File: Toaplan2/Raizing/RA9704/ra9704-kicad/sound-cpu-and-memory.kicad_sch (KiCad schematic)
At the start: 10 parts, among them U713 74HC244, U717 74HC367, U74 74HC244, U75 TMPZ84C00AP-8 (Z80), U77 27C020, U78 CY7C185

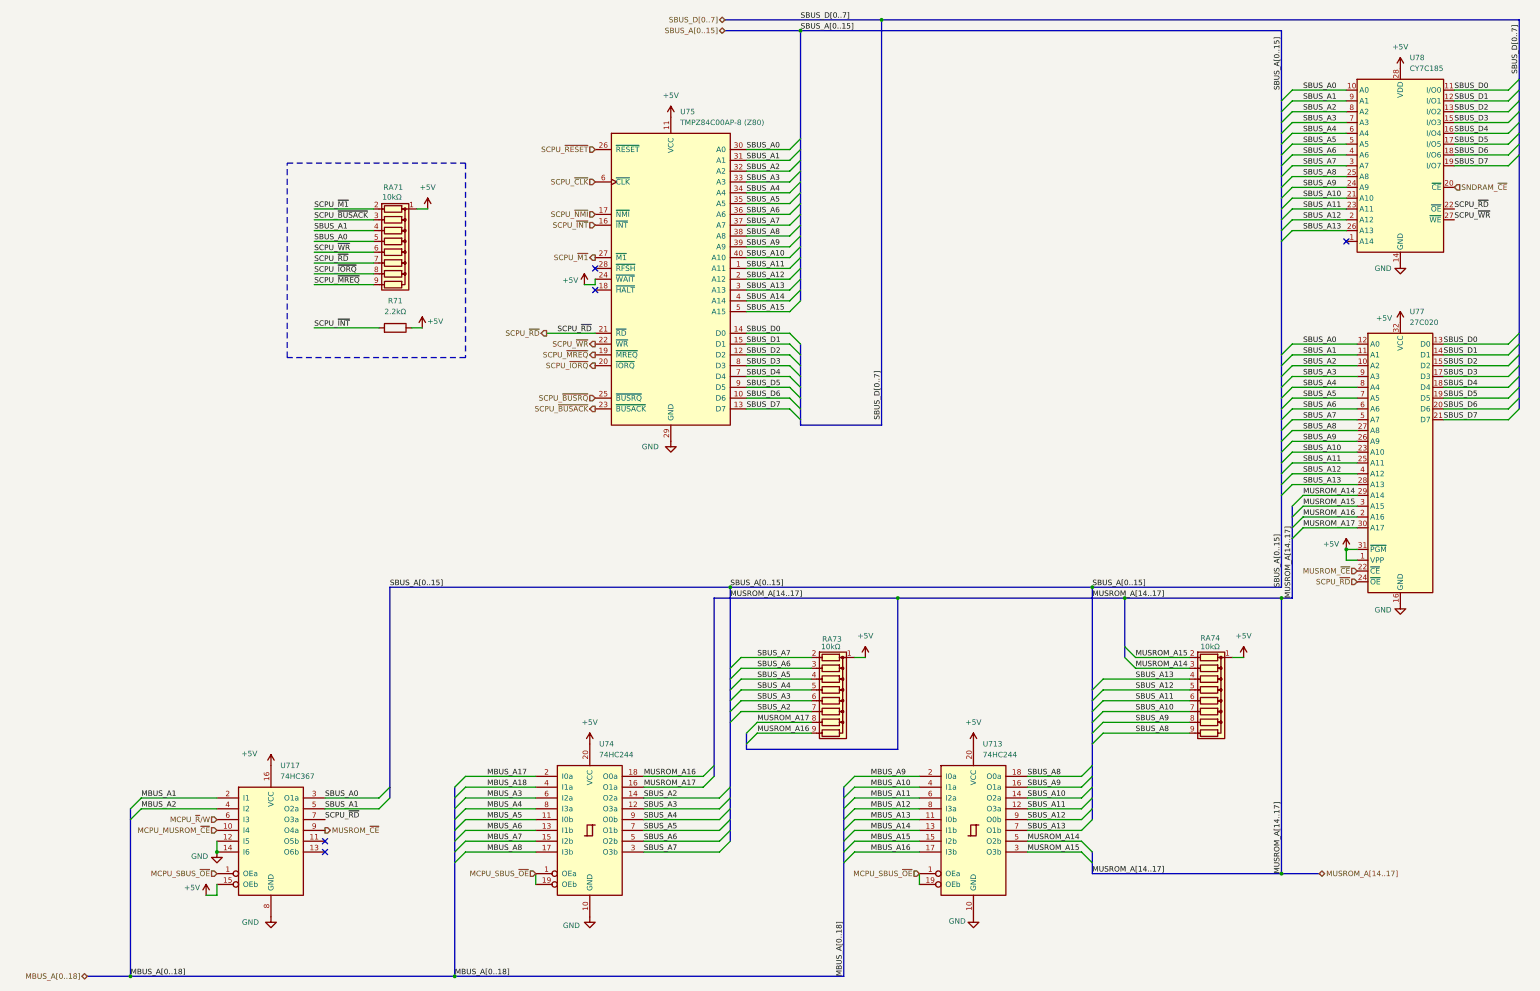
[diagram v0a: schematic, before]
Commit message: fix(ra9704): Add Os as a proxy for 0s in all reference designators
RA9704 has reference designators such that each number has a preceding zero (e.g. RA076, U074, etc.). This causes a bug in KiCAD.

This is 'fixed' by using the 'O' (the letter 'Oh') character instead.

For more info, see the following issue on the KiCAD Gitlab repo

https://gitlab.com/kicad/code/kicad/-/issues/19229
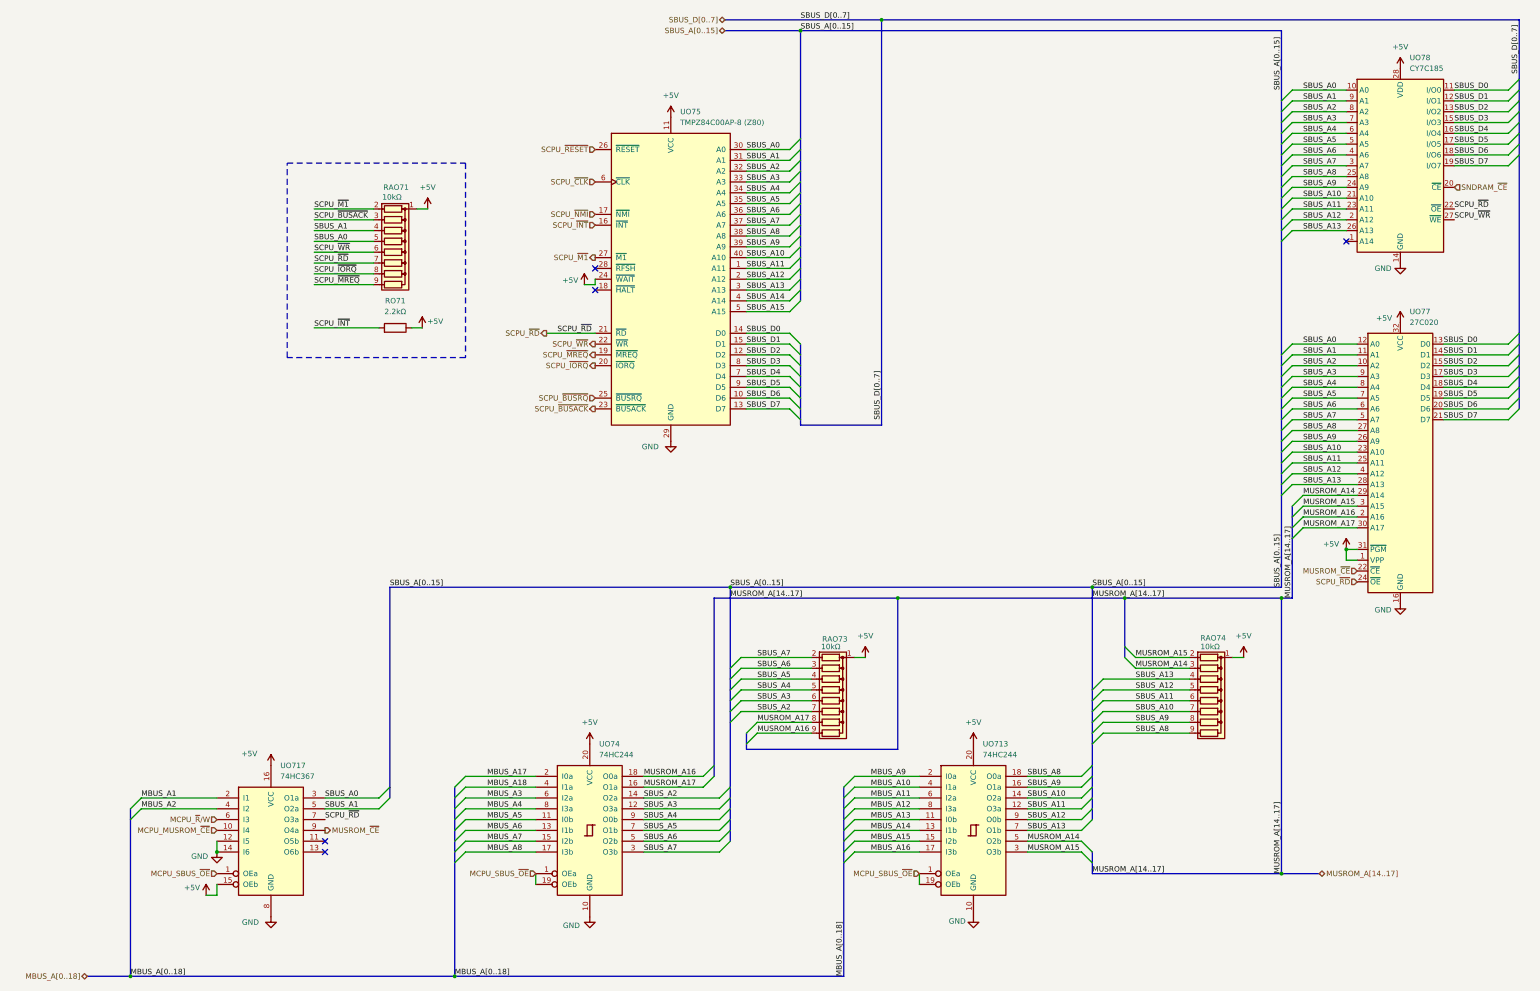
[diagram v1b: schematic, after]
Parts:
- renumbered RA71 to RAO71, RA73 to RAO73, RA74 to RAO74, R71 to RO71, U713 to UO713, U717 to UO717, U74 to UO74, U75 to UO75, U77 to UO77, U78 to UO78
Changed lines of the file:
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@@
 		(dnp no)
 		(fields_autoplaced yes)
-		(property "Reference" "U713"
+		(property "Reference" "UO713"
 			(at 267.6241 189.23 0)
 			(effects
@@
 			(project "ra9704"
 				(path "/24d3b4cf-2360-45fc-8c40-cedc8afdf9e1/44ef47a8-0f29-401a-8a6a-1ae8d653f277"
-					(reference "U713")
+					(reference "UO713")
 					(unit 1)
 				)
@@
 		(dnp no)
 		(fields_autoplaced yes)
-		(property "Reference" "U77"
+		(property "Reference" "UO77"
 			(at 367.9541 87.63 0)
 			(effects
@@
 			(project "ra9704"
 				(path "/24d3b4cf-2360-45fc-8c40-cedc8afdf9e1/44ef47a8-0f29-401a-8a6a-1ae8d653f277"
-					(reference "U77")
+					(reference "UO77")
 					(unit 1)
 				)
@@
 		(on_board yes)
 		(dnp no)
-		(property "Reference" "RA74"
+		(property "Reference" "RAO74"
 			(at 318.77 164.338 90)
 			(effects
@@
 			(project "ra9704"
 				(path "/24d3b4cf-2360-45fc-8c40-cedc8afdf9e1/44ef47a8-0f29-401a-8a6a-1ae8d653f277"
-					(reference "RA74")
+					(reference "RAO74")
 					(unit 1)
 				)
@@
 		(on_board yes)
 		(dnp no)
-		(property "Reference" "RA71"
+		(property "Reference" "RAO71"
 			(at 126.746 58.42 90)
 			(effects
@@
 			(project "ra9704"
 				(path "/24d3b4cf-2360-45fc-8c40-cedc8afdf9e1/44ef47a8-0f29-401a-8a6a-1ae8d653f277"
-					(reference "RA71")
+					(reference "RAO71")
 					(unit 1)
 				)
@@
 		(dnp no)
 		(fields_autoplaced yes)
-		(property "Reference" "U75"
+		(property "Reference" "UO75"
 			(at 196.5041 40.64 0)
 			(effects
@@
 			(project "ra9704"
 				(path "/24d3b4cf-2360-45fc-8c40-cedc8afdf9e1/44ef47a8-0f29-401a-8a6a-1ae8d653f277"
-					(reference "U75")
+					(reference "UO75")
 					(unit 1)
 				)
@@
 		(dnp no)
 		(fields_autoplaced yes)
-		(property "Reference" "U74"
+		(property "Reference" "UO74"
 			(at 177.4541 189.23 0)
 			(effects
@@
 			(project "ra9704"
 				(path "/24d3b4cf-2360-45fc-8c40-cedc8afdf9e1/44ef47a8-0f29-401a-8a6a-1ae8d653f277"
-					(reference "U74")
+					(reference "UO74")
 					(unit 1)
 				)
@@
 		(dnp no)
 		(fields_autoplaced yes)
-		(property "Reference" "U78"
+		(property "Reference" "UO78"
 			(at 367.9541 27.94 0)
 			(effects
@@
 			(project "ra9704"
 				(path "/24d3b4cf-2360-45fc-8c40-cedc8afdf9e1/44ef47a8-0f29-401a-8a6a-1ae8d653f277"
-					(reference "U78")
+					(reference "UO78")
 					(unit 1)
 				)
@@
 		(on_board yes)
 		(dnp no)
-		(property "Reference" "RA73"
+		(property "Reference" "RAO73"
 			(at 229.87 164.592 90)
 			(effects
@@
 			(project "ra9704"
 				(path "/24d3b4cf-2360-45fc-8c40-cedc8afdf9e1/44ef47a8-0f29-401a-8a6a-1ae8d653f277"
-					(reference "RA73")
+					(reference "RAO73")
 					(unit 1)
 				)
@@
 		(dnp no)
 		(fields_autoplaced yes)
-		(property "Reference" "R71"
+		(property "Reference" "RO71"
 			(at 129.54 85.09 90)
 			(effects
@@
 			(project "ra9704"
 				(path "/24d3b4cf-2360-45fc-8c40-cedc8afdf9e1/44ef47a8-0f29-401a-8a6a-1ae8d653f277"
-					(reference "R71")
+					(reference "RO71")
 					(unit 1)
 				)
@@
 		(dnp no)
 		(fields_autoplaced yes)
-		(property "Reference" "U717"
+		(property "Reference" "UO717"
 			(at 102.5241 194.31 0)
 			(effects
@@
 			(project "ra9704"
 				(path "/24d3b4cf-2360-45fc-8c40-cedc8afdf9e1/44ef47a8-0f29-401a-8a6a-1ae8d653f277"
-					(reference "U717")
-					(unit 1)
-				)
+					(reference "UO717")
+					(unit 1)
+				)
